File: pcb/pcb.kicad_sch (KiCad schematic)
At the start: 113 parts, among them J1 MJ-4PP-9, J2 MJ-4PP-9, J3 USB_C_Receptacle_USB2.0_16P, J4 USB to TTL, J5 Conn_01x03, J6 Conn_01x03, SW1 KEY_SW, SW10 KEY_SW, SW11 KEY_SW, SW12 KEY_SW, SW13 KEY_SW, SW14 KEY_SW, SW15 KEY_SW, SW16 KEY_SW, SW17 KEY_SW, SW18 KEY_SW, SW19 KEY_SW, SW2 KEY_SW, SW20 KEY_SW, SW21 KEY_SW, SW22 KEY_SW, SW23 KEY_SW, SW24 KEY_SW, SW25 KEY_SW, SW26 KEY_SW, SW27 RotaryEncoder, SW3 KEY_SW, SW30 KEY_SW, SW31 KEY_SW, SW32 KEY_SW, SW33 KEY_SW, SW34 KEY_SW, SW35 KEY_SW, SW36 KEY_SW, SW37 KEY_SW, SW38 KEY_SW, SW39 KEY_SW, SW4 KEY_SW, SW40 KEY_SW, SW41 KEY_SW, SW42 KEY_SW, SW43 KEY_SW, SW44 KEY_SW, SW45 KEY_SW, SW46 KEY_SW, SW47 KEY_SW, SW48 KEY_SW, SW49 KEY_SW, SW5 KEY_SW, SW50 KEY_SW, SW51 KEY_SW, SW52 KEY_SW, SW53 KEY_SW, SW54 KEY_SW, SW6 KEY_SW, SW60 RESET_SW, SW61 BOOT_SW, SW7 KEY_SW, SW8 KEY_SW, SW9 KEY_SW, SW６２1 DIP_SW, U1 ESP32-S3-WROOM-1, U2 TPS1117LV33S, U3 USBLC6-2SC6

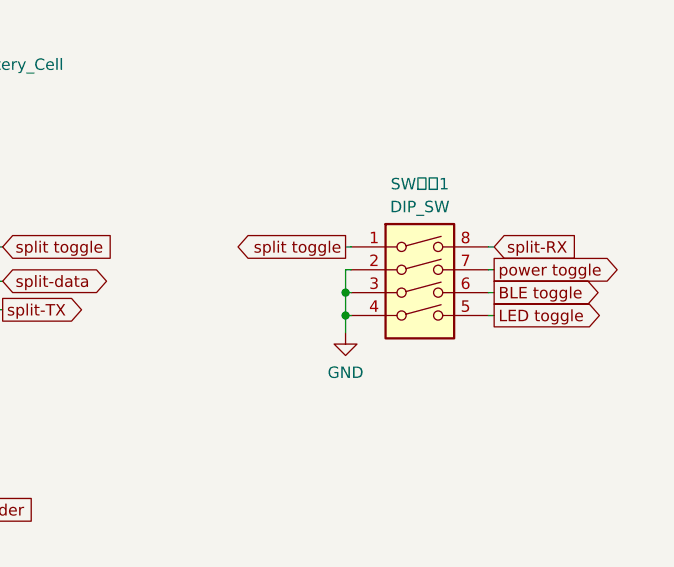
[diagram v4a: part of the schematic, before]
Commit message: switch put to pcb
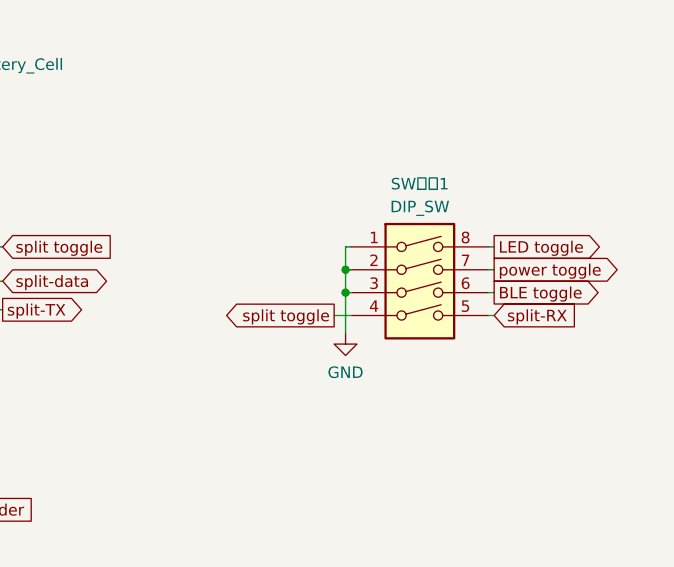
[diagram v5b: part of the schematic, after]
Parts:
- C1, C2: footprint lib:StripLED_rev -> Capacitor_SMD:C_0805_2012Metric_Pad1.18x1.45mm_HandSolder
- C3, C4, C6, C7: footprint (none) -> Capacitor_SMD:C_0805_2012Metric_Pad1.18x1.45mm_HandSolder
- C5: footprint (none) -> Capacitor_SMD:C_0603_1608Metric_Pad1.08x0.95mm_HandSolder
- LED1, LED2, LED3, LED4, LED5: footprint kbd:YS-SK6812MINI-E -> lib:YS-SK6812MINI-E
- U2: footprint (none) -> Package_TO_SOT_SMD:SOT-223-3_TabPin2
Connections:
- net GND: now also SW６２1.1; no longer SW６２1.4
- net LED toggle: now also SW６２1.8; no longer SW６２1.5
- net split toggle: now also SW６２1.4; no longer SW６２1.1
- net split-RX: now also SW６２1.5; no longer SW６２1.8
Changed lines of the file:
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@@
 	)
 	(junction
+		(at 299.72 224.79)
+		(diameter 0)
+		(color 0 0 0 0)
+	)
+	(junction
 		(at 148.59 100.33)
 		(diameter 0)
@@
 	)
 	(junction
-		(at 299.72 224.79)
-		(diameter 0)
-		(color 0 0 0 0)
-	)
-	(junction
 		(at 233.68 167.005)
 		(diameter 0)
@@
 	)
 	(junction
-		(at 299.72 227.33)
+		(at 299.72 222.25)
 		(diameter 0)
 		(color 0 0 0 0)
@@
 	(wire
 		(pts
+			(xy 299.72 229.235) (xy 299.72 224.79)
+		)
+		(stroke
+			(width 0)
+			(type default)
+		)
+	)
+	(wire
+		(pts
 			(xy 234.95 120.65) (xy 234.95 132.08)
 		)
@@
 	(wire
 		(pts
+			(xy 298.45 227.33) (xy 300.355 227.33)
+		)
+		(stroke
+			(width 0)
+			(type default)
+		)
+	)
+	(wire
+		(pts
 			(xy 234.95 19.05) (xy 234.95 25.4)
 		)
@@
 	(wire
 		(pts
+			(xy 299.72 219.71) (xy 299.72 222.25)
+		)
+		(stroke
+			(width 0)
+			(type default)
+		)
+	)
+	(wire
+		(pts
 			(xy 199.39 57.15) (xy 199.39 68.58)
 		)
@@
 	(wire
 		(pts
-			(xy 299.72 224.79) (xy 299.72 227.33)
-		)
-		(stroke
-			(width 0)
-			(type default)
-		)
-	)
-	(wire
-		(pts
 			(xy 143.51 230.505) (xy 153.67 230.505)
 		)
@@
 	(wire
 		(pts
-			(xy 299.72 227.33) (xy 300.355 227.33)
-		)
-		(stroke
-			(width 0)
-			(type default)
-		)
-	)
-	(wire
-		(pts
 			(xy 133.35 88.9) (xy 133.35 100.33)
 		)
@@
 	(wire
 		(pts
-			(xy 299.72 229.235) (xy 299.72 227.33)
-		)
-		(stroke
-			(width 0)
-			(type default)
-		)
-	)
-	(wire
-		(pts
 			(xy 111.125 250.19) (xy 112.395 250.19)
 		)
@@
 	(global_label "LED toggle"
 		(shape output)
-		(at 316.23 227.33 0)
+		(at 316.23 219.71 0)
 		(fields_autoplaced yes)
 		(effects
@@
 		)
 		(property "Intersheetrefs" "${INTERSHEET_REFS}"
-			(at 329.5564 227.33 0)
+			(at 329.5564 219.71 0)
 			(effects
 				(font
@@
 	(global_label "split toggle"
 		(shape output)
-		(at 299.72 219.71 180)
+		(at 298.45 227.33 180)
 		(fields_autoplaced yes)
 		(effects
@@
 		)
 		(property "Intersheetrefs" "${INTERSHEET_REFS}"
-			(at 285.6679 219.71 0)
+			(at 284.3979 227.33 0)
 			(effects
 				(font
@@
 	(global_label "split-RX"
 		(shape input)
-		(at 316.23 219.71 0)
+		(at 316.23 227.33 0)
 		(fields_autoplaced yes)
 		(effects
@@
 		)
 		(property "Intersheetrefs" "${INTERSHEET_REFS}"
-			(at 327.4399 219.71 0)
+			(at 327.4399 227.33 0)
 			(effects
 				(font
@@
 			)
 		)
-		(property "Footprint" "lib:StripLED_rev"
+		(property "Footprint" "Capacitor_SMD:C_0805_2012Metric_Pad1.18x1.45mm_HandSolder"
 			(at 70.7898 224.79 0)
 			(effects
@@
 			)
 		)
-		(property "Footprint" "kbd:YS-SK6812MINI-E"
+		(property "Footprint" "lib:YS-SK6812MINI-E"
 			(at 259.715 164.465 0)
 			(effects
@@
 			)
 		)
-		(property "Footprint" "kbd:YS-SK6812MINI-E"
+		(property "Footprint" "lib:YS-SK6812MINI-E"
 			(at 236.22 164.465 0)
 			(effects
@@
 			)
 		)
-		(property "Footprint" "kbd:YS-SK6812MINI-E"
+		(property "Footprint" "lib:YS-SK6812MINI-E"
 			(at 212.725 164.465 0)
 			(effects
@@
 			)
 		)
-		(property "Footprint" "lib:StripLED_rev"
+		(property "Footprint" "Capacitor_SMD:C_0805_2012Metric_Pad1.18x1.45mm_HandSolder"
 			(at 57.15 233.3498 0)
 			(effects
@@
 			)
 		)
-		(property "Footprint" ""
+		(property "Footprint" "Capacitor_SMD:C_0603_1608Metric_Pad1.08x0.95mm_HandSolder"
 			(at 230.2002 265.43 0)
 			(effects
@@
 			)
 		)
-		(property "Footprint" "kbd:YS-SK6812MINI-E"
+		(property "Footprint" "lib:YS-SK6812MINI-E"
 			(at 165.735 164.465 0)
 			(effects
@@
 			)
 		)
-		(property "Footprint" ""
+		(property "Footprint" "Capacitor_SMD:C_0805_2012Metric_Pad1.18x1.45mm_HandSolder"
 			(at 202.8698 201.295 0)
 			(effects
@@
 			)
 		)
-		(property "Footprint" ""
+		(property "Footprint" "Capacitor_SMD:C_0805_2012Metric_Pad1.18x1.45mm_HandSolder"
 			(at 179.3748 201.295 0)
 			(effects
@@
 			)
 		)
-		(property "Footprint" ""
+		(property "Footprint" "Capacitor_SMD:C_0805_2012Metric_Pad1.18x1.45mm_HandSolder"
 			(at 220.0402 201.295 0)
 			(effects
@@
 			)
 		)
-		(property "Footprint" "kbd:YS-SK6812MINI-E"
+		(property "Footprint" "lib:YS-SK6812MINI-E"
 			(at 189.23 164.465 0)
 			(effects
@@
 			)
 		)
-		(property "Footprint" ""
+		(property "Footprint" "Capacitor_SMD:C_0805_2012Metric_Pad1.18x1.45mm_HandSolder"
 			(at 191.4398 201.295 0)
 			(effects
@@
 			)
 		)
-		(property "Footprint" ""
+		(property "Footprint" "Package_TO_SOT_SMD:SOT-223-3_TabPin2"
 			(at 211.455 187.325 0)
 			(effects

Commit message: ESP32 put to pcb
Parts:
- C1, C2: footprint Capacitor_SMD:C_0805_2012Metric_Pad1.18x1.45mm_HandSolder -> lib:C_0805_2012Metric_Pad1.18x1.45mm_HandSolder_rev
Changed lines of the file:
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@@
 			)
 		)
-		(property "Footprint" "Capacitor_SMD:C_0805_2012Metric_Pad1.18x1.45mm_HandSolder"
+		(property "Footprint" "lib:C_0805_2012Metric_Pad1.18x1.45mm_HandSolder_rev"
 			(at 70.7898 224.79 0)
 			(effects
@@
 			)
 		)
-		(property "Footprint" "Capacitor_SMD:C_0805_2012Metric_Pad1.18x1.45mm_HandSolder"
+		(property "Footprint" "lib:C_0805_2012Metric_Pad1.18x1.45mm_HandSolder_rev"
 			(at 57.15 233.3498 0)
 			(effects

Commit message: connect
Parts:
- J3: footprint Connector_USB:USB_C_Receptacle_GCT_USB4105-xx-A_16P_TopMnt_Horizontal -> lib:USB_C_Receptacle_GCT_USB4105-xx-A_16P_TopMnt_Horizontal_rev
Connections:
- net BLE toggle: now also U1.7 (IO7); no longer U1.18 (IO10)
- net LED toggle: now also U1.6 (IO6); no longer U1.19 (IO11)
- net col1: now also U1.39 (IO1); no longer U1.15 (IO3)
- net col2: now also U1.21 (IO13); no longer U1.4 (IO4)
- net col3: now also U1.20 (IO12); no longer U1.5 (IO5)
- net col4: now also U1.19 (IO11); no longer U1.6 (IO6)
- net col5: now also U1.18 (IO10); no longer U1.7 (IO7)
- net col6: now also U1.17 (IO9); no longer U1.12 (IO8)
- net power toggle: now also U1.12 (IO8); no longer U1.17 (IO9)
- net slider: now also U1.15 (IO3); no longer U1.39 (IO1)
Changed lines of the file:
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@@
 	)
 	(no_connect
-		(at 142.875 240.03)
+		(at 111.125 242.57)
 	)
 	(no_connect
-		(at 112.395 260.35)
+		(at 142.875 240.03)
 	)
 	(no_connect
@@
 	)
 	(no_connect
-		(at 112.395 262.89)
+		(at 112.395 270.51)
 	)
 	(no_connect
-		(at 112.395 270.51)
+		(at 111.125 240.03)
 	)
 	(no_connect
@@
 	(wire
 		(pts
+			(xy 111.125 260.35) (xy 112.395 260.35)
+		)
+		(stroke
+			(width 0)
+			(type default)
+		)
+	)
+	(wire
+		(pts
 			(xy 254 186.055) (xy 254 187.325)
 		)
@@
 	(wire
 		(pts
+			(xy 12.7 6.35) (xy 12.7 5.08)
+		)
+		(stroke
+			(width 0)
+			(type default)
+		)
+	)
+	(wire
+		(pts
 			(xy 60.96 234.315) (xy 57.15 234.315)
 		)
@@
 	(wire
 		(pts
+			(xy 111.125 262.89) (xy 112.395 262.89)
+		)
+		(stroke
+			(width 0)
+			(type default)
+		)
+	)
+	(wire
+		(pts
 			(xy 233.68 149.225) (xy 233.68 150.495)
 		)
@@
 	(wire
 		(pts
+			(xy 4.445 6.35) (xy 4.445 5.08)
+		)
+		(stroke
+			(width 0)
+			(type default)
+		)
+	)
+	(wire
+		(pts
 			(xy 176.53 254) (xy 177.8 254)
 		)
@@
 		)
 	)
+	(label "VBUS"
+		(at 12.7 5.08 0)
+		(fields_autoplaced yes)
+		(effects
+			(font
+				(size 1.27 1.27)
+			)
+			(justify left bottom)
+		)
+	)
 	(global_label "col5"
 		(shape output)
@@
 	(global_label "LED toggle"
 		(shape input)
-		(at 111.125 257.81 180)
+		(at 111.125 245.11 180)
 		(fields_autoplaced yes)
 		(effects
@@
 		)
 		(property "Intersheetrefs" "${INTERSHEET_REFS}"
-			(at 97.7986 257.81 0)
+			(at 97.7986 245.11 0)
 			(effects
 				(font
@@
 	(global_label "col6"
 		(shape input)
-		(at 111.125 250.19 180)
+		(at 111.125 252.73 180)
 		(fields_autoplaced yes)
 		(effects
@@
 		)
 		(property "Intersheetrefs" "${INTERSHEET_REFS}"
-			(at 104.0275 250.19 0)
+			(at 104.0275 252.73 0)
 			(effects
 				(font
@@
 	(global_label "BLE toggle"
 		(shape input)
-		(at 111.125 255.27 180)
+		(at 111.125 247.65 180)
 		(fields_autoplaced yes)
 		(effects
@@
 		)
 		(property "Intersheetrefs" "${INTERSHEET_REFS}"
-			(at 97.7986 255.27 0)
+			(at 97.7986 247.65 0)
 			(effects
 				(font
@@
 	(global_label "power toggle"
 		(shape input)
-		(at 111.125 252.73 180)
+		(at 111.125 250.19 180)
 		(fields_autoplaced yes)
 		(effects
@@
 		)
 		(property "Intersheetrefs" "${INTERSHEET_REFS}"
-			(at 95.7424 252.73 0)
+			(at 95.7424 250.19 0)
 			(effects
 				(font
@@
 	(global_label "col2"
 		(shape input)
-		(at 111.125 240.03 180)
+		(at 111.125 262.89 180)
 		(fields_autoplaced yes)
 		(effects
@@
 		)
 		(property "Intersheetrefs" "${INTERSHEET_REFS}"
-			(at 104.0275 240.03 0)
+			(at 104.0275 262.89 0)
 			(effects
 				(font
@@
 	(global_label "col3"
 		(shape input)
-		(at 111.125 242.57 180)
+		(at 111.125 260.35 180)
 		(fields_autoplaced yes)
 		(effects
@@
 		)
 		(property "Intersheetrefs" "${INTERSHEET_REFS}"
-			(at 104.0275 242.57 0)
+			(at 104.0275 260.35 0)
 			(effects
 				(font
@@
 	(global_label "col5"
 		(shape input)
-		(at 111.125 247.65 180)
+		(at 111.125 255.27 180)
 		(fields_autoplaced yes)
 		(effects
@@
 		)
 		(property "Intersheetrefs" "${INTERSHEET_REFS}"
-			(at 104.0275 247.65 0)
+			(at 104.0275 255.27 0)
 			(effects
 				(font
@@
 	(global_label "col1"
 		(shape input)
-		(at 111.125 237.49 180)
+		(at 111.125 232.41 180)
 		(fields_autoplaced yes)
 		(effects
@@
 		)
 		(property "Intersheetrefs" "${INTERSHEET_REFS}"
-			(at 104.0275 237.49 0)
+			(at 104.0275 232.41 0)
 			(effects
 				(font
@@
 	(global_label "col4"
 		(shape input)
-		(at 111.125 245.11 180)
+		(at 111.125 257.81 180)
 		(fields_autoplaced yes)
 		(effects
@@
 		)
 		(property "Intersheetrefs" "${INTERSHEET_REFS}"
-			(at 104.0275 245.11 0)
+			(at 104.0275 257.81 0)
 			(effects
 				(font
@@
 	(global_label "slider"
 		(shape output)
-		(at 111.125 232.41 180)
+		(at 111.125 237.49 180)
 		(fields_autoplaced yes)
 		(effects
@@
 		)
 		(property "Intersheetrefs" "${INTERSHEET_REFS}"
-			(at 102.8179 232.41 0)
+			(at 102.8179 237.49 0)
 			(effects
 				(font
@@
 	)
 	(symbol
-		(lib_id "power:VCC")
-		(at 12.7 5.08 0)
-		(unit 1)
-		(exclude_from_sim no)
-		(in_bom yes)
-		(on_board yes)
-		(dnp no)
-		(property "Reference" "#PWR05"
-			(at 12.7 8.89 0)
-			(effects
-				(font
-					(size 1.27 1.27)
-				)
-				(hide yes)
-			)
-		)
-		(property "Value" "VCC"
-			(at 12.7 1.27 0)
-			(effects
-				(font
-					(size 1.27 1.27)
-				)
-			)
-		)
-		(property "Footprint" ""
-			(at 12.7 5.08 0)
-			(effects
-				(font
-					(size 1.27 1.27)
-				)
-				(hide yes)
-			)
-		)
-		(property "Datasheet" ""
-			(at 12.7 5.08 0)
-			(effects
-				(font
-					(size 1.27 1.27)
-				)
-				(hide yes)
-			)
-		)
-		(property "Description" ""
-			(at 12.7 5.08 0)
-			(effects
-				(font
-					(size 1.27 1.27)
-				)
-				(hide yes)
-			)
-		)
-		(pin "1"
-		)
-		(instances
-			(project "pcb"
-				(path "/ca1682eb-af97-4baf-a70b-d30c3b256c66"
-					(reference "#PWR05")
-					(unit 1)
-				)
-			)
-		)
-	)
-	(symbol
 		(lib_id "Device:D")
 		(at 173.99 104.14 90)
@@
 			)
 		)
-		(property "Footprint" "Connector_USB:USB_C_Receptacle_GCT_USB4105-xx-A_16P_TopMnt_Horizontal"
+		(property "Footprint" "lib:USB_C_Receptacle_GCT_USB4105-xx-A_16P_TopMnt_Horizontal_rev"
 			(at 207.645 234.95 0)
 			(effects
@@
 	(symbol
 		(lib_id "power:PWR_FLAG")
-		(at 5.08 5.08 0)
+		(at 4.445 5.08 0)
 		(unit 1)
 		(exclude_from_sim no)
@@
 		(dnp no)
 		(property "Reference" "#FLG01"
-			(at 5.08 3.175 0)
+			(at 4.445 3.175 0)
 			(effects
 				(font
@@
 		)
 		(property "Value" "PWR_FLAG"
-			(at 5.08 1.27 0)
+			(at 4.445 1.27 0)
 			(effects
 				(font
@@
 		)
 		(property "Footprint" ""
-			(at 5.08 5.08 0)
+			(at 4.445 5.08 0)
 			(effects
 				(font
@@
 		)
 		(property "Datasheet" "~"
-			(at 5.08 5.08 0)
+			(at 4.445 5.08 0)
 			(effects
 				(font
@@
 		)
 		(property "Description" ""
-			(at 5.08 5.08 0)
+			(at 4.445 5.08 0)
 			(effects
 				(font
@@
 	(symbol
 		(lib_id "power:GND")
-		(at 5.08 5.08 0)
+		(at 4.445 6.35 0)
 		(unit 1)
 		(exclude_from_sim no)
@@
 		(dnp no)
 		(property "Reference" "#PWR04"
-			(at 5.08 11.43 0)
+			(at 4.445 12.7 0)
 			(effects
 				(font
@@
 		)
 		(property "Value" "GND"
-			(at 5.08 8.89 0)
+			(at 4.445 10.16 0)
 			(effects
 				(font
@@
 		)
 		(property "Footprint" ""
-			(at 5.08 5.08 0)
+			(at 4.445 6.35 0)
 			(effects
 				(font
@@
 		)
 		(property "Datasheet" ""
-			(at 5.08 5.08 0)
+			(at 4.445 6.35 0)
 			(effects
 				(font
@@
 		)
 		(property "Description" ""
-			(at 5.08 5.08 0)
+			(at 4.445 6.35 0)
 			(effects
 				(font
@@
 	(symbol
 		(lib_id "power:PWR_FLAG")
-		(at 12.7 5.08 180)
+		(at 12.7 6.35 180)
 		(unit 1)
 		(exclude_from_sim no)
@@
 		(dnp no)
 		(property "Reference" "#FLG02"
-			(at 12.7 6.985 0)
+			(at 12.7 8.255 0)
 			(effects
 				(font
@@
 		)
 		(property "Value" "PWR_FLAG"
-			(at 12.7 8.89 0)
+			(at 12.7 10.16 0)
 			(effects
 				(font
@@
 		)
 		(property "Footprint" ""
-			(at 12.7 5.08 0)
+			(at 12.7 6.35 0)
 			(effects
 				(font
@@
 		)
 		(property "Datasheet" "~"
-			(at 12.7 5.08 0)
+			(at 12.7 6.35 0)
 			(effects
 				(font
@@
 		)
 		(property "Description" ""
-			(at 12.7 5.08 0)
+			(at 12.7 6.35 0)
 			(effects
 				(font

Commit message: fix DRC error of switch
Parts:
- SW10, SW11, SW12, SW13, SW14, SW22, SW23, SW24, SW25, SW26, SW8, SW9: footprint kbd:keyswitch_cherrymx_hotswap_1u -> lib:keyswitch_cherrymx_hotswap_1u_no_hole
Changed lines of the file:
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@@
 			)
 		)
-		(property "Footprint" "kbd:keyswitch_cherrymx_hotswap_1u"
+		(property "Footprint" "lib:keyswitch_cherrymx_hotswap_1u_no_hole"
 			(at 191.77 132.08 0)
 			(effects
@@
 			)
 		)
-		(property "Footprint" "kbd:keyswitch_cherrymx_hotswap_1u"
+		(property "Footprint" "lib:keyswitch_cherrymx_hotswap_1u_no_hole"
 			(at 217.17 68.58 0)
 			(effects
@@
 			)
 		)
-		(property "Footprint" "kbd:keyswitch_cherrymx_hotswap_1u"
+		(property "Footprint" "lib:keyswitch_cherrymx_hotswap_1u_no_hole"
 			(at 115.57 132.08 0)
 			(effects
@@
 			)
 		)
-		(property "Footprint" "kbd:keyswitch_cherrymx_hotswap_1u"
+		(property "Footprint" "lib:keyswitch_cherrymx_hotswap_1u_no_hole"
 			(at 217.17 132.08 0)
 			(effects
@@
 			)
 		)
-		(property "Footprint" "kbd:keyswitch_cherrymx_hotswap_1u"
+		(property "Footprint" "lib:keyswitch_cherrymx_hotswap_1u_no_hole"
 			(at 140.97 68.58 0)
 			(effects
@@
 			)
 		)
-		(property "Footprint" "kbd:keyswitch_cherrymx_hotswap_1u"
+		(property "Footprint" "lib:keyswitch_cherrymx_hotswap_1u_no_hole"
 			(at 166.37 68.58 0)
 			(effects
@@
 			)
 		)
-		(property "Footprint" "kbd:keyswitch_cherrymx_hotswap_1u"
+		(property "Footprint" "lib:keyswitch_cherrymx_hotswap_1u_no_hole"
 			(at 242.57 68.58 0)
 			(effects
@@
 			)
 		)
-		(property "Footprint" "kbd:keyswitch_cherrymx_hotswap_1u"
+		(property "Footprint" "lib:keyswitch_cherrymx_hotswap_1u_no_hole"
 			(at 115.57 68.58 0)
 			(effects
@@
 			)
 		)
-		(property "Footprint" "kbd:keyswitch_cherrymx_hotswap_1u"
+		(property "Footprint" "lib:keyswitch_cherrymx_hotswap_1u_no_hole"
 			(at 191.77 68.58 0)
 			(effects
@@
 			)
 		)
-		(property "Footprint" "kbd:keyswitch_cherrymx_hotswap_1u"
+		(property "Footprint" "lib:keyswitch_cherrymx_hotswap_1u_no_hole"
 			(at 242.57 132.08 0)
 			(effects
@@
 			)
 		)
-		(property "Footprint" "kbd:keyswitch_cherrymx_hotswap_1u"
+		(property "Footprint" "lib:keyswitch_cherrymx_hotswap_1u_no_hole"
 			(at 267.97 132.08 0)
 			(effects
@@
 			)
 		)
-		(property "Footprint" "kbd:keyswitch_cherrymx_hotswap_1u"
+		(property "Footprint" "lib:keyswitch_cherrymx_hotswap_1u_no_hole"
 			(at 267.97 68.58 0)
 			(effects
